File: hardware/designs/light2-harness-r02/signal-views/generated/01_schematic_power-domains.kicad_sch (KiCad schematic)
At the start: 45 parts, among them J2 ESP32-P4 Right Header (EXT1), J3 ESP32-P4 Left Header (EXT2), U1 SN74LVC244AN, U2 SN74LVC244AN, U3 SN74LV125AN, U4 SN74LV125AN

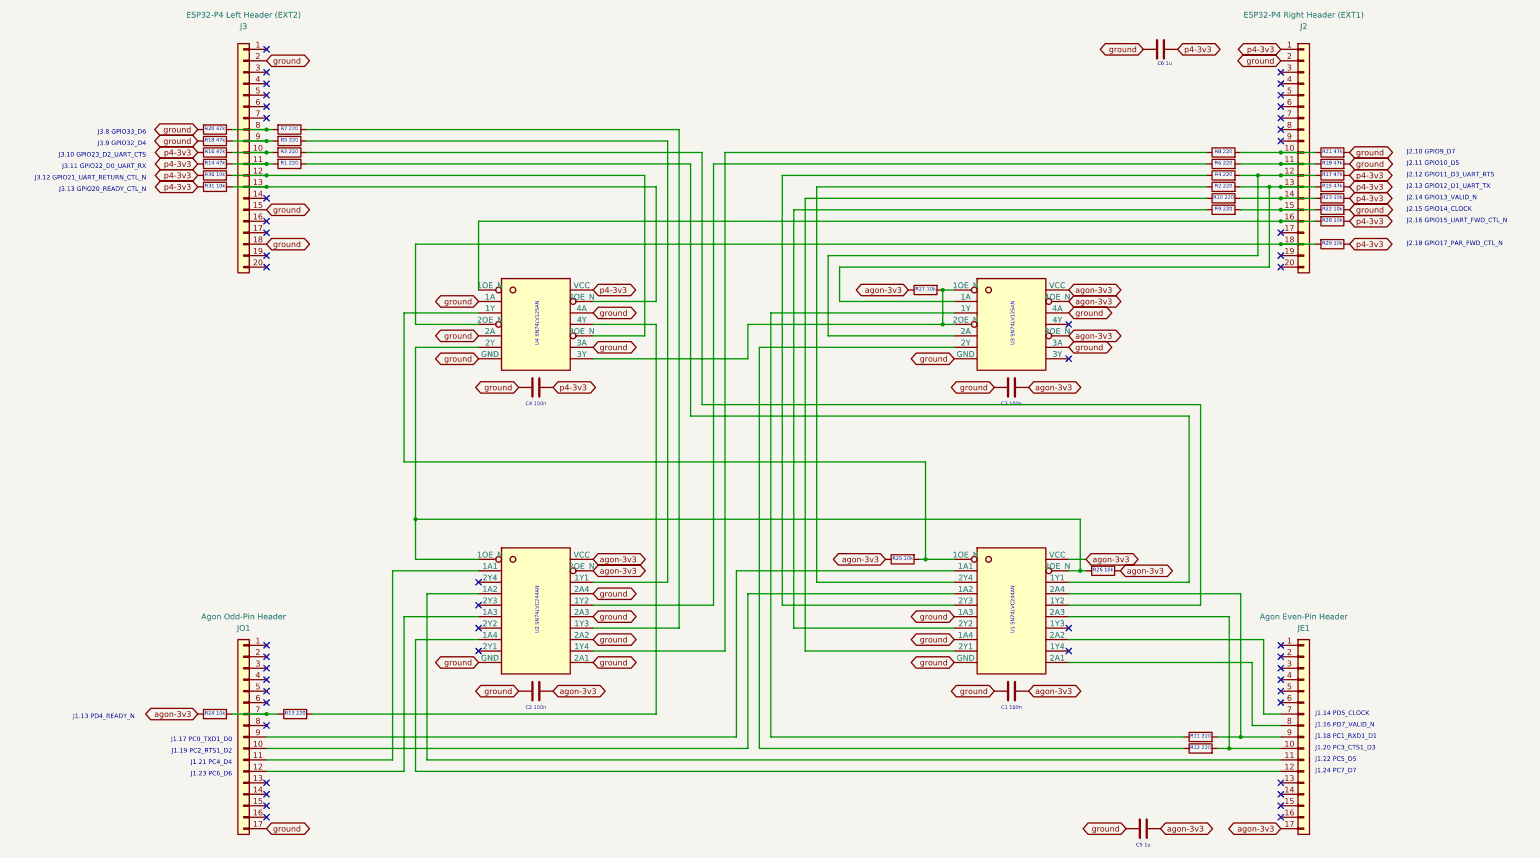
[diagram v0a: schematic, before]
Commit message: HW-001: freeze r02 schematic and ordered signal views
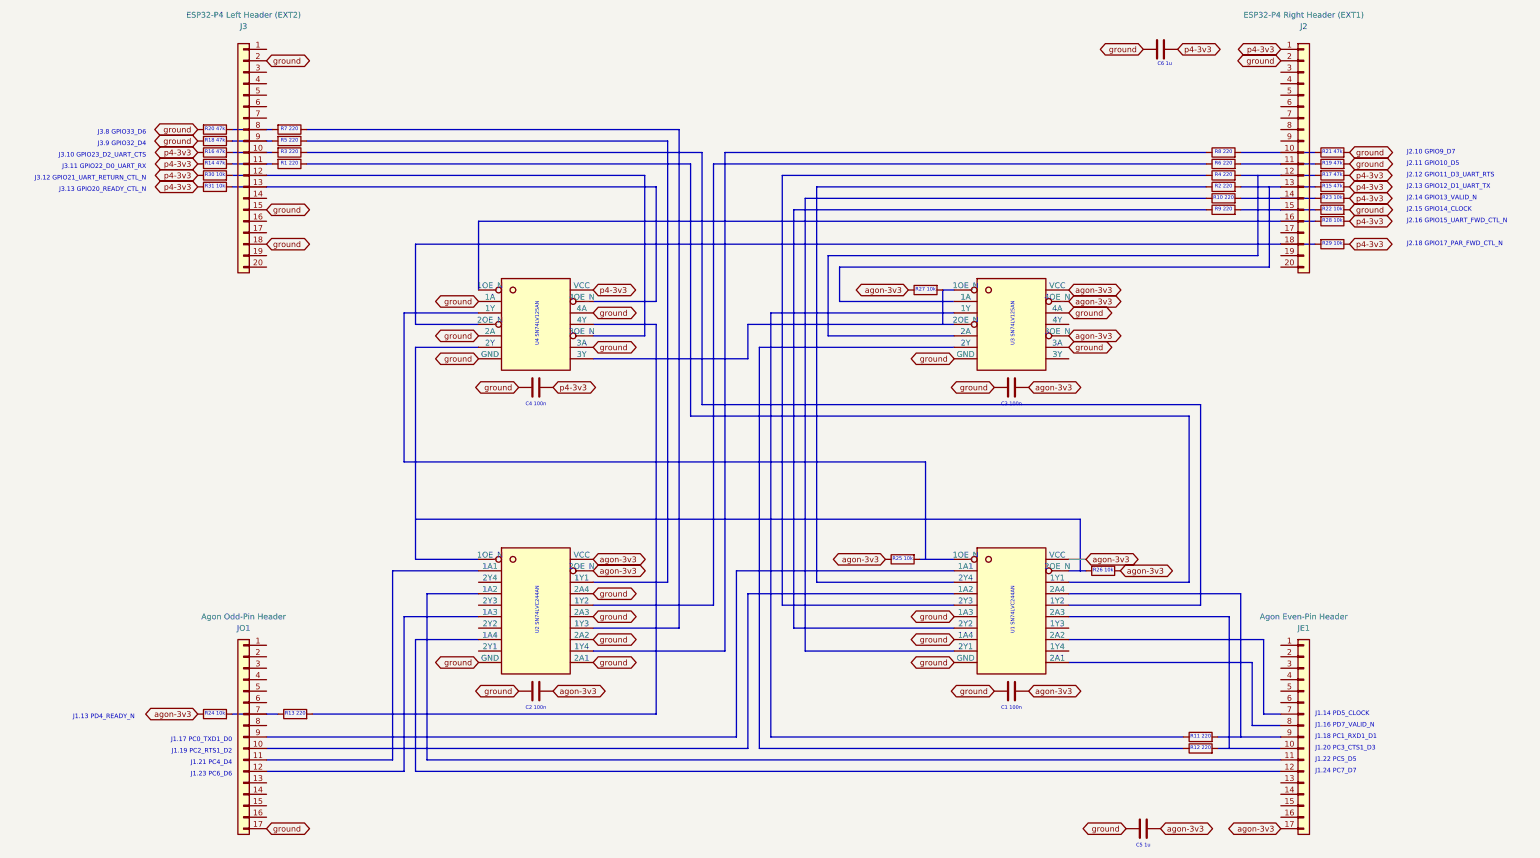
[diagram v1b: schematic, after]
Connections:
- net at R11.1: no longer U3.3 (1Y)
- net at R5.1: no longer U2.18 (1Y1)
- net at R13.2: no longer U4.11 (4Y)
- net at R6.1: no longer U2.16 (1Y2)
- net at R7.1: no longer U2.14 (1Y3)
- net at U2.12 (1Y4): no longer R8.1
- net at U2.2 (1A1): no longer JO1.11 (Pin_11)
- net at U2.4 (1A2): no longer JE1.11 (Pin_11)
- net at U2.6 (1A3): no longer JO1.12 (Pin_12)
- net at U2.8 (1A4): no longer JE1.12 (Pin_12)
- net at R3.1: no longer U1.16 (1Y2)
- net at R1.1: no longer U1.18 (1Y1)
- net at R2.1: no longer U1.3 (2Y4)
- net at R10.1: no longer U1.9 (2Y1)
- net at R12.1: no longer U3.6 (2Y)
- net at R4.1: no longer U1.5 (2Y3)
- net at R9.1: no longer U1.7 (2Y2)
- net at JO1.10 (Pin_10): no longer U1.4 (1A2)
- net at JO1.9 (Pin_9): no longer U1.2 (1A1)
- net at JE1.7 (Pin_7): no longer U1.13 (2A2)
- net at JE1.8 (Pin_8): no longer U1.11 (2A1)
- now unconnected: J2.10 (Pin_10), J2.11 (Pin_11), J2.12 (Pin_12), J2.13 (Pin_13), J2.14 (Pin_14), J2.15 (Pin_15), J2.16 (Pin_16), J2.18 (Pin_18), J3.10 (Pin_10), J3.11 (Pin_11), J3.12 (Pin_12), J3.13 (Pin_13), J3.8 (Pin_8), J3.9 (Pin_9), JE1.10 (Pin_10), JE1.9 (Pin_9), JO1.7 (Pin_7), R1.2, R10.2, R11.2, R12.2, R13.1, R14.2, R15.2, R16.2, R17.2, R18.1, R19.1, R2.2, R20.1, R21.1, R22.1, R23.2, R24.2, R25.2, R26.2, R27.2, R28.2, R29.2, R3.2, R30.2, R31.2, R4.2, R5.2, R6.2, R7.2, R8.2, R9.2, U1.1 (1OE_N), U1.15 (2A3), U1.17 (2A4), U1.19 (2OE_N), U2.1 (1OE_N), U3.1 (1OE_N), U3.2 (1A), U3.4 (2OE_N), U3.5 (2A), U4.1 (1OE_N), U4.10 (3OE_N), U4.13 (4OE_N), U4.3 (1Y), U4.4 (2OE_N), U4.6 (2Y), U4.8 (3Y)
- no-connect marks 50 -> 0
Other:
- title: Light 2 harness r02 — PHYSICAL TOP-VIEW DIP DIRECT-WIRE AID -> Light 2 harness r02 — Power domains and common ground — FUNCTION VIEW, NOT AUTHORITY
